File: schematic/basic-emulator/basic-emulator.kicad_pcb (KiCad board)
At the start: 2 copper layers, 44.2 x 61.7 mm, 14 parts

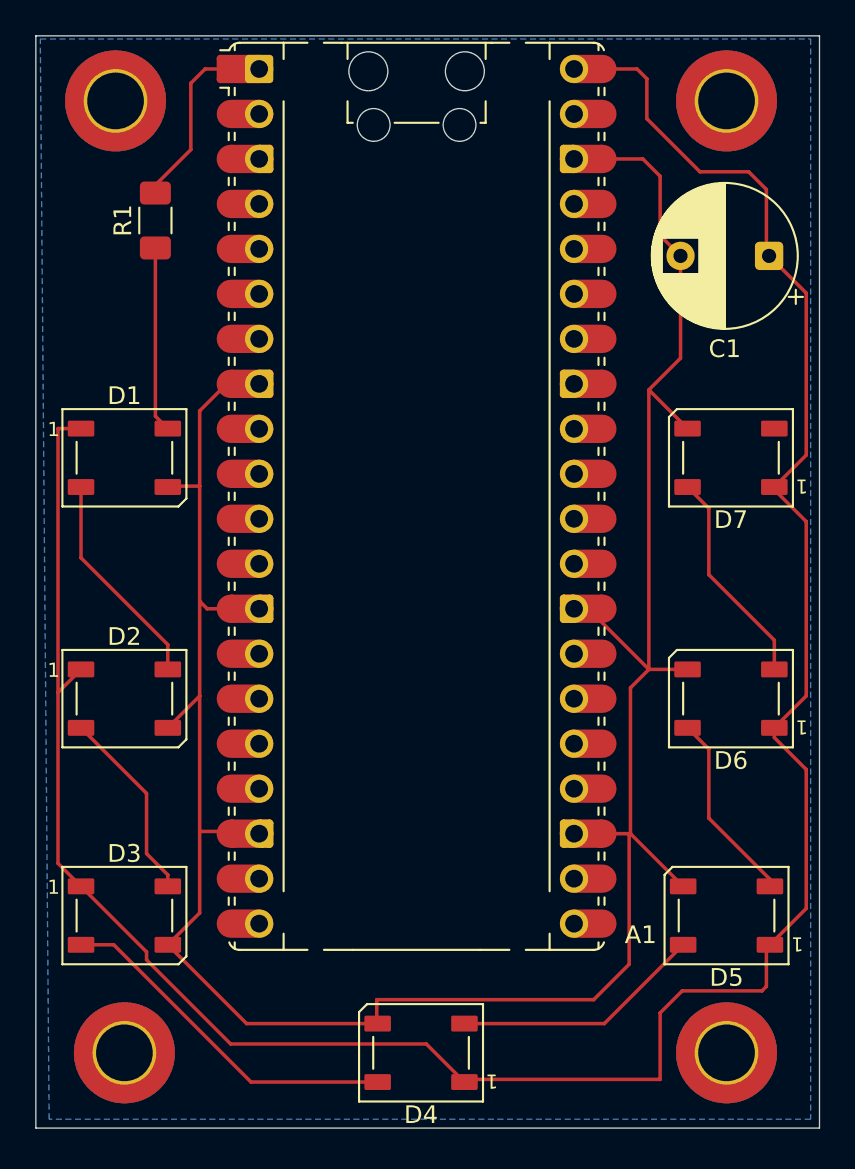
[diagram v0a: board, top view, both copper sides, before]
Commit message: Add websockets support for colors + extra packets
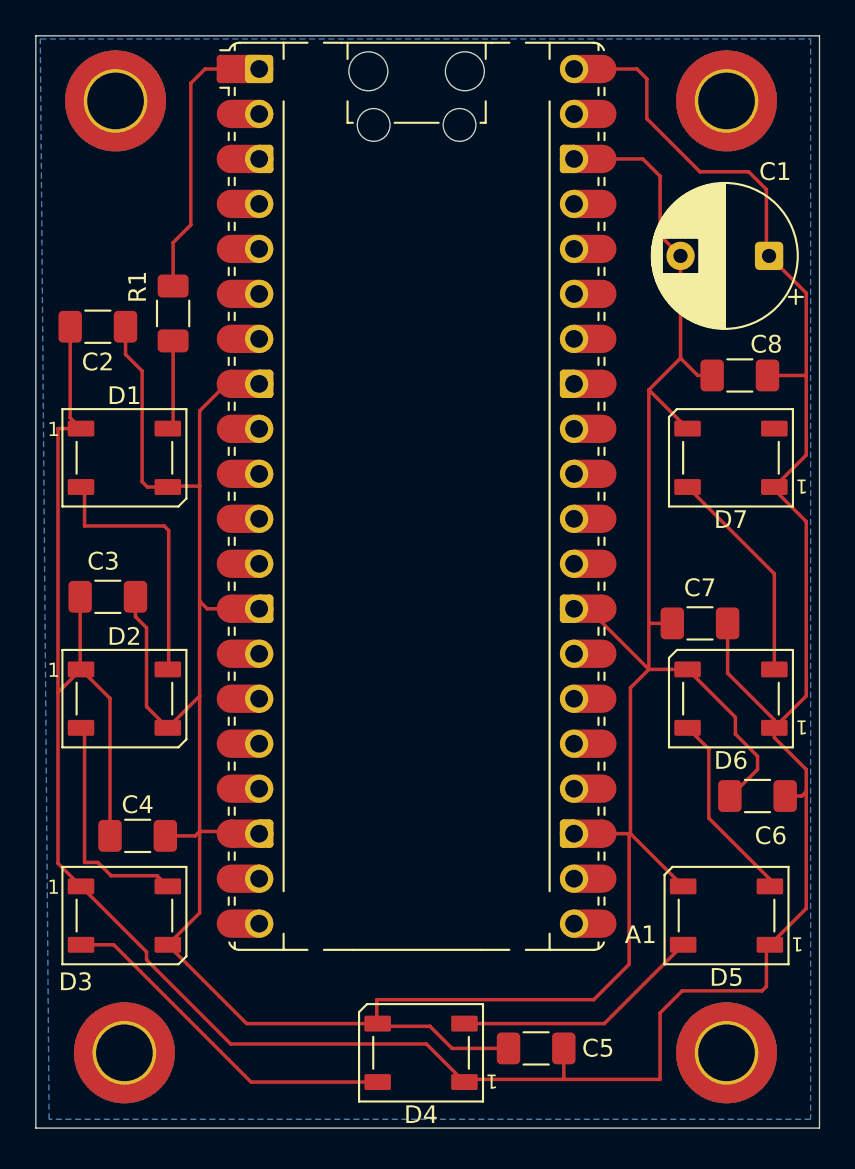
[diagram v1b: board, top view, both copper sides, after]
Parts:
- added C2: 104, Capacitor_SMD:C_1206_3216Metric_Pad1.33x1.80mm_HandSolder, F.Cu at (155.0, 69.0)
- added C3: 104, Capacitor_SMD:C_1206_3216Metric_Pad1.33x1.80mm_HandSolder, F.Cu at (155.6, 84.2)
- added C4: 104, Capacitor_SMD:C_1206_3216Metric_Pad1.33x1.80mm_HandSolder, F.Cu at (157.2, 97.8)
- added C5: 104, Capacitor_SMD:C_1206_3216Metric_Pad1.33x1.80mm_HandSolder, F.Cu at (179.8, 109.8)
- added C6: 104, Capacitor_SMD:C_1206_3216Metric_Pad1.33x1.80mm_HandSolder, F.Cu at (192.2, 95.5)
- added C7: 104, Capacitor_SMD:C_1206_3216Metric_Pad1.33x1.80mm_HandSolder, F.Cu at (189.0, 85.8)
- added C8: 104, Capacitor_SMD:C_1206_3216Metric_Pad1.33x1.80mm_HandSolder, F.Cu at (191.2, 71.8)
- moved R1 5.34 mm to (159.2, 68.2)
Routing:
- net GND: track 146.1 -> 188.1 mm
- net +5V: track 142.3 -> 174.8 mm
- net Net-(D1-DIN): track 10.5 -> 5.07 mm
- net Net-(A1-GPIO0): track 11.2 -> 16.1 mm
- net Net-(D1-DOUT): track 12.3 -> 15.0 mm
- net Net-(D2-DOUT): track 11.0 -> 12.9 mm
